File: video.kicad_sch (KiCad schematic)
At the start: 52 parts, among them IC103 HUC6260, IC108 μPC358C

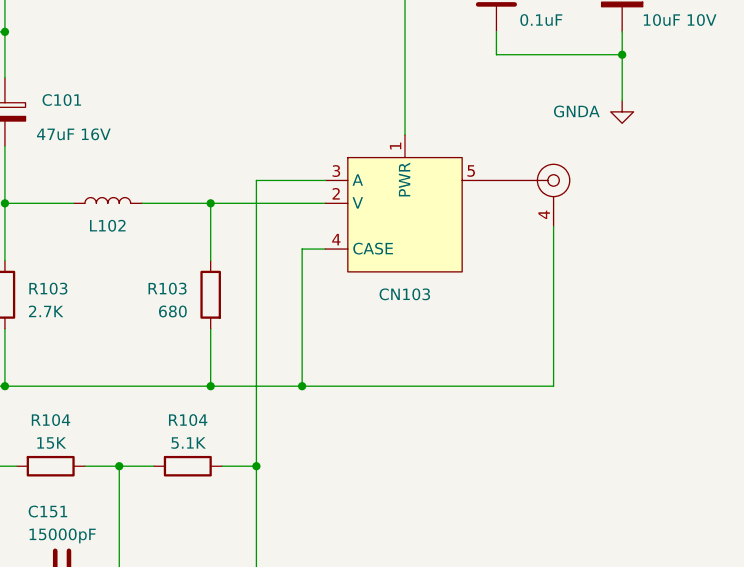
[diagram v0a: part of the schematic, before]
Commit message: Remove some sharp corners on traces, generate BOM.
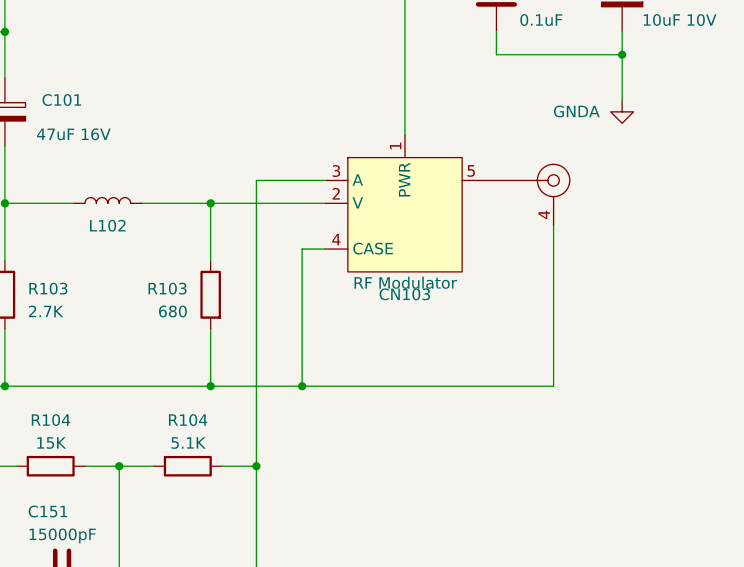
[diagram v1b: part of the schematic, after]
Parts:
- CN103: value ~ -> RF Modulator
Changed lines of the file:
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@@
       (effects (font (size 1.27 1.27)))
     )
-    (property "Value" "~" (at 328.93 129.54 0)
+    (property "Value" "RF Modulator" (at 328.93 129.54 0)
       (effects (font (size 1.27 1.27)))
     )
